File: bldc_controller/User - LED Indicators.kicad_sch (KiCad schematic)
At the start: 4 parts

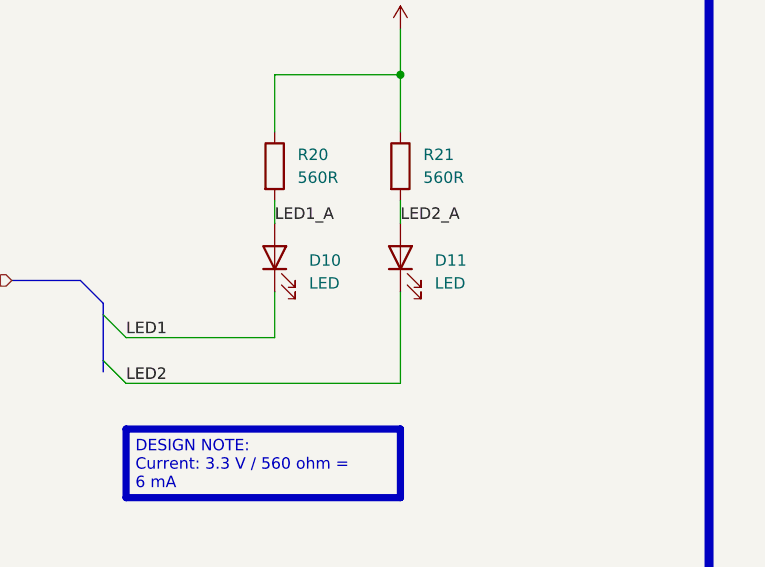
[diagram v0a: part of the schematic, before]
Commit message: schematic is complete. Replaced 5V buck and added pi filters.
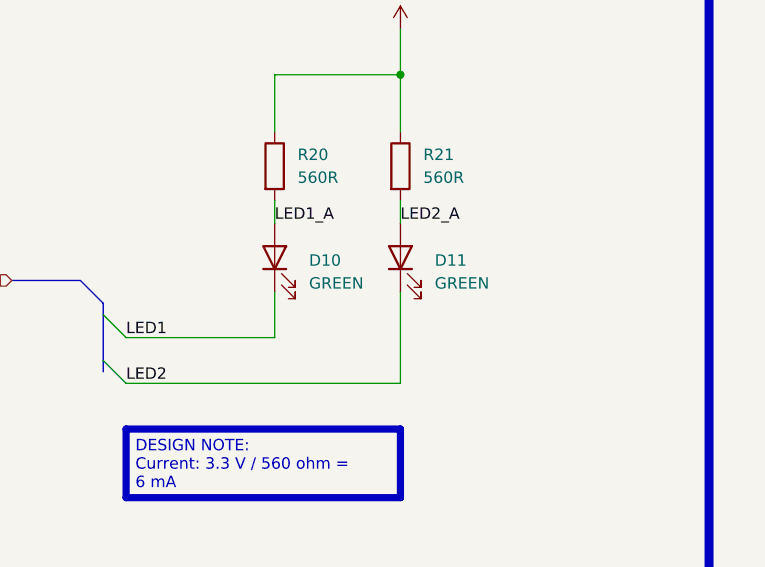
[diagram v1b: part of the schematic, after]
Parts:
- D10, D11: value LED -> GREEN
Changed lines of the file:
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@@
       (effects (font (size 1.27 1.27)) (justify right))
     )
-    (property "Value" "LED" (at 166.37 91.7575 90)
+    (property "Value" "GREEN" (at 166.37 91.7575 90)
       (effects (font (size 1.27 1.27)) (justify right))
     )
@@
       (effects (font (size 1.27 1.27)) (justify right))
     )
-    (property "Value" "LED" (at 152.4 91.7575 90)
+    (property "Value" "GREEN" (at 152.4 91.7575 90)
       (effects (font (size 1.27 1.27)) (justify right))
     )

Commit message: added assembly files
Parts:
- R20, R21: value 560R -> 560R 1%
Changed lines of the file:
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@@
       (effects (font (size 1.27 1.27)) (justify left))
     )
-    (property "Value" "560R" (at 165.1 80.01 0)
+    (property "Value" "560R 1%" (at 165.1 80.01 0)
       (effects (font (size 1.27 1.27)) (justify left))
     )
@@
       (effects (font (size 1.27 1.27)) (justify left))
     )
-    (property "Value" "560R" (at 151.13 80.01 0)
+    (property "Value" "560R 1%" (at 151.13 80.01 0)
       (effects (font (size 1.27 1.27)) (justify left))
     )
